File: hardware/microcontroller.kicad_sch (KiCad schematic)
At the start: 11 parts, among them U1 STM32G474QBT6

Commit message: Very minor schematic tweaks
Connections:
- net VUSB SENSE renamed VUSB_SENSE
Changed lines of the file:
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@@
+		)
+	)
+	(label "VUSB_SENSE"
+		(at 147.32 45.72 0)
+		(effects
+			(font
+				(size 1.27 1.27)
+			)
+			(justify left bottom)
 		)
 	)
@@
 		)
 	)
-	(label "VUSB SENSE"
-		(at 147.32 45.72 0)
-		(effects
-			(font
-				(size 1.27 1.27)
-			)
-			(justify left bottom)
-		)
-	)
 	(label "SWDIO"
 		(at 129.54 60.96 180)
@@
 		)
 	)
-	(label "VUSB SENSE"
+	(label "VUSB_SENSE"
 		(at 129.54 48.26 180)
 		(effects

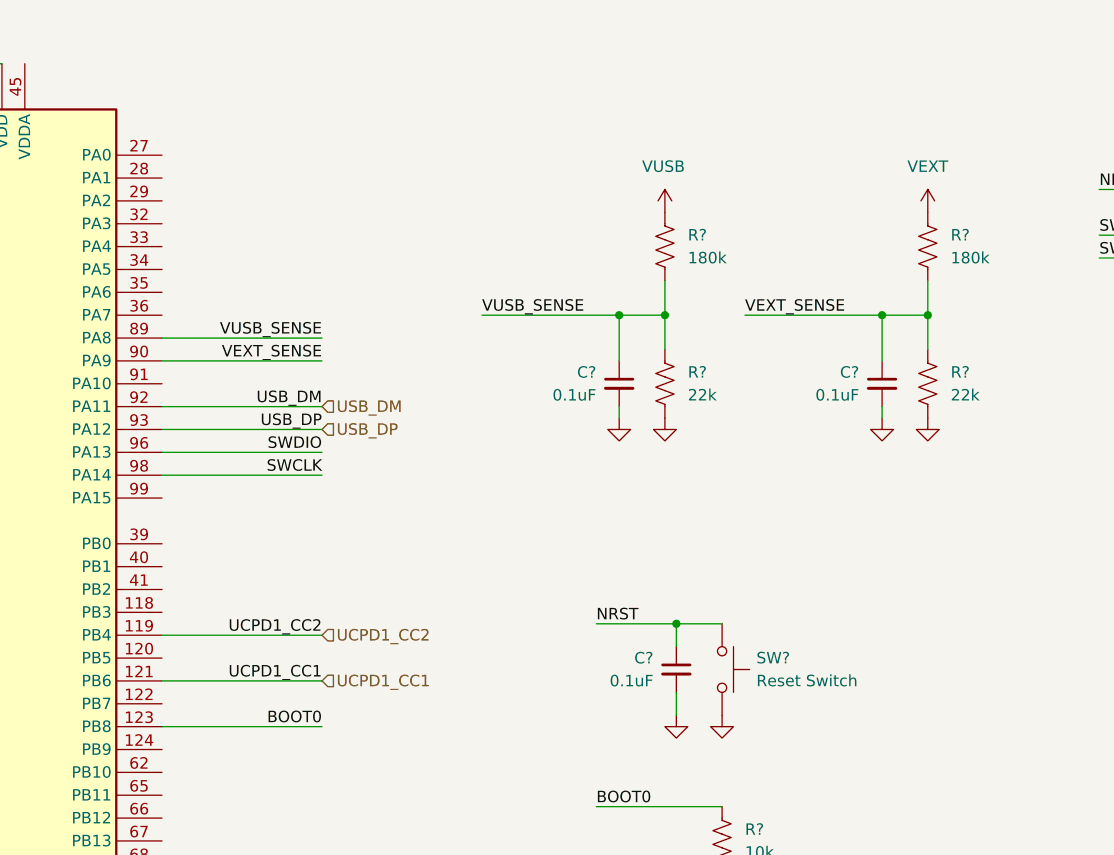
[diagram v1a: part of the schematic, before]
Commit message: Remove USB C PD and refine power input
Deleted USB C PD features due to complexity. Simplified power input schematic. Sourced PSU, connectors, crimps, and created external harness schematics.
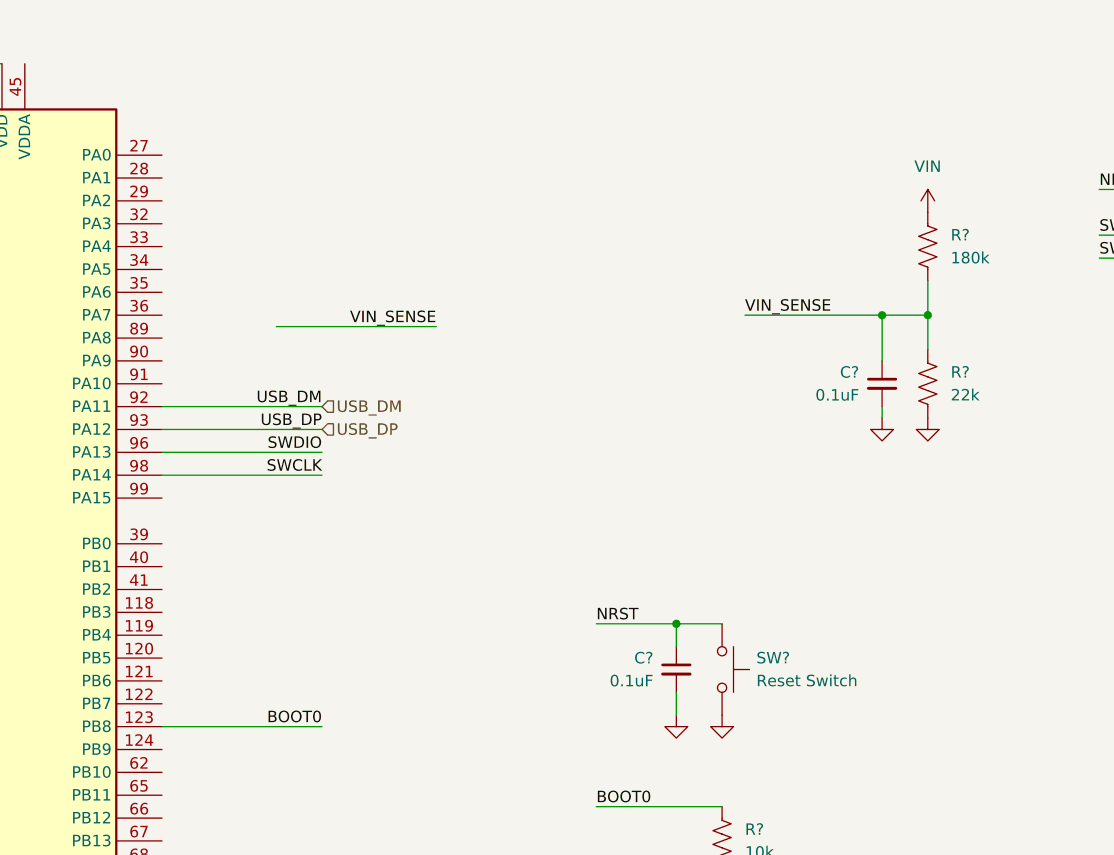
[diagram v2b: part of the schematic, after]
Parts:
- removed C?: 0.1uF, Capacitor_SMD:C_0603_1608Metric_Pad1.08x0.95mm_HandSolder, symbol Device:C_Small
- removed R?: 180k, symbol Device:R_US
- removed R?: 22k, symbol Device:R_US
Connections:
- net UCPD1_CC1: no longer names the net of U1.121 (PB6)
- net UCPD1_CC2: no longer names the net of U1.119 (PB4)
- net VEXT renamed VIN
- net VEXT_SENSE renamed VIN_SENSE
- net VIN_SENSE: no longer U1.90 (PA9)
- net VUSB_SENSE: no longer names the net of U1.89 (PA8)

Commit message: Finish power input
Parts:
- R?: footprint (none) -> Resistor_SMD:R_0603_1608Metric; Part Number (none) -> RC0603FR-0710KL; Vendor URL (none) -> https://www.digikey.com/en/products/detail/yageo/RC0603FR-0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
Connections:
- net VIN renamed VMOTOR
- net VIN_SENSE renamed VMOTOR_SENSE
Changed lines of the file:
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@@
 		)
 	)
-	(label "VIN_SENSE"
+	(label "VMOTOR_SENSE"
 		(at 176.53 45.72 0)
 		(effects
@@
 		)
 	)
+	(label "VMOTOR_SENSE"
+		(at 142.24 46.99 180)
+		(effects
+			(font
+				(size 1.27 1.27)
+			)
+			(justify right bottom)
+		)
+	)
 	(label "HSE_OSC_IN"
 		(at 38.1 66.04 0)
@@
 	(label "SWDIO"
 		(at 129.54 60.96 180)
-		(effects
-			(font
-				(size 1.27 1.27)
-			)
-			(justify right bottom)
-		)
-	)
-	(label "VIN_SENSE"
-		(at 142.24 46.99 180)
 		(effects
 			(font
@@
 	)
 	(symbol
+		(lib_id "power:VBUS")
+		(at 196.85 34.29 0)
+		(unit 1)
+		(body_style 1)
+		(exclude_from_sim no)
+		(in_bom yes)
+		(on_board yes)
+		(in_pos_files yes)
+		(dnp no)
+		(fields_autoplaced yes)
+		(property "Reference" "#PWR05"
+			(at 196.85 38.1 0)
+			(hide yes)
+			(show_name no)
+			(do_not_autoplace no)
+			(effects
+				(font
+					(size 1.27 1.27)
+				)
+			)
+		)
+		(property "Value" "VMOTOR"
+			(at 196.85 29.21 0)
+			(show_name no)
+			(do_not_autoplace no)
+			(effects
+				(font
+					(size 1.27 1.27)
+				)
+			)
+		)
+		(property "Footprint" ""
+			(at 196.85 34.29 0)
+			(hide yes)
+			(show_name no)
+			(do_not_autoplace no)
+			(effects
+				(font
+					(size 1.27 1.27)
+				)
+			)
+		)
+		(property "Datasheet" ""
+			(at 196.85 34.29 0)
+			(hide yes)
+			(show_name no)
+			(do_not_autoplace no)
+			(effects
+				(font
+					(size 1.27 1.27)
+				)
+			)
+		)
+		(property "Description" "Power symbol creates a global label with name \"VBUS\""
+			(at 196.85 34.29 0)
+			(hide yes)
+			(show_name no)
+			(do_not_autoplace no)
+			(effects
+				(font
+					(size 1.27 1.27)
+				)
+			)
+		)
+		(pin "1"
+		)
+		(instances
+			(project "stepping-stone"
+				(path "/793a882e-3f7b-468b-a863-41a1f527e1bf/d2f9d032-a5e5-45d0-b37f-4be86e3babb1"
+					(reference "#PWR05")
+					(unit 1)
+				)
+			)
+		)
+	)
+	(symbol
 		(lib_id "Device:R_US")
 		(at 196.85 38.1 0)
@@
 				(path "/793a882e-3f7b-468b-a863-41a1f527e1bf/d2f9d032-a5e5-45d0-b37f-4be86e3babb1"
 					(reference "R?")
-					(unit 1)
-				)
-			)
-		)
-	)
-	(symbol
-		(lib_id "power:VBUS")
-		(at 196.85 34.29 0)
-		(unit 1)
-		(body_style 1)
-		(exclude_from_sim no)
-		(in_bom yes)
-		(on_board yes)
-		(in_pos_files yes)
-		(dnp no)
-		(property "Reference" "#PWR035"
-			(at 196.85 38.1 0)
-			(hide yes)
-			(show_name no)
-			(do_not_autoplace no)
-			(effects
-				(font
-					(size 1.27 1.27)
-				)
-			)
-		)
-		(property "Value" "VIN"
-			(at 196.85 29.21 0)
-			(show_name no)
-			(do_not_autoplace no)
-			(effects
-				(font
-					(size 1.27 1.27)
-				)
-			)
-		)
-		(property "Footprint" ""
-			(at 196.85 34.29 0)
-			(hide yes)
-			(show_name no)
-			(do_not_autoplace no)
-			(effects
-				(font
-					(size 1.27 1.27)
-				)
-			)
-		)
-		(property "Datasheet" ""
-			(at 196.85 34.29 0)
-			(hide yes)
-			(show_name no)
-			(do_not_autoplace no)
-			(effects
-				(font
-					(size 1.27 1.27)
-				)
-			)
-		)
-		(property "Description" "Power symbol creates a global label with name \"VBUS\""
-			(at 196.85 34.29 0)
-			(hide yes)
-			(show_name no)
-			(do_not_autoplace no)
-			(effects
-				(font
-					(size 1.27 1.27)
-				)
-			)
-		)
-		(pin "1"
-		)
-		(instances
-			(project "stepping-stone"
-				(path "/793a882e-3f7b-468b-a863-41a1f527e1bf/d2f9d032-a5e5-45d0-b37f-4be86e3babb1"
-					(reference "#PWR035")
 					(unit 1)
 				)
@@
 			)
 		)
-		(property "Footprint" ""
+		(property "Footprint" "Resistor_SMD:R_0603_1608Metric"
 			(at 175.006 104.394 90)
 			(hide yes)
@@
 			)
 		)
-		(property "Datasheet" ""
+		(property "Datasheet" "https://yageogroup.com/content/datasheet/asset/file/PYU-RC_GROUP_51_ROHS_L"
 			(at 173.99 104.14 0)
 			(hide yes)
@@
 			(at 173.99 104.14 0)
 			(hide yes)
+			(show_name no)
+			(do_not_autoplace no)
+			(effects
+				(font
+					(size 1.27 1.27)
+				)
+			)
+		)
+		(property "Part Number" "RC0603FR-0710KL"
+			(at 173.99 104.14 0)
+			(hide yes)
+			(show_name no)
+			(do_not_autoplace no)
+			(effects
+				(font
+					(size 1.27 1.27)
+				)
+			)
+		)
+		(property "Vendor URL" "https://www.digikey.com/en/products/detail/yageo/RC0603FR-0710KL/726880"
+			(at 173.99 104.14 0)
+			(hide yes)

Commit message: Update LEDs
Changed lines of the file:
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@@
+		)
+	)
+	(hierarchical_label "USB_STATUS"
+		(shape output)
+		(at 135.89 50.8 0)
+		(effects
+			(font
+				(size 1.27 1.27)
+			)
+			(justify left)
 		)
 	)

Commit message: Connector Updates
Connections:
- net SWO: now reaches J?.8 (JTDO/SWO)
- net SWO: now also U1.118 (PB3)
- no-connect marks 5 -> 4
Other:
- note added: "Connector Search"

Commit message: Complete TMC2209 sheet
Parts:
- J?: footprint Connector_PinHeader_1.27mm:PinHeader_2x07_P1.27mm_Vertical_SMD -> Connector_PinHeader_1.27mm:PinHeader_2x07_P1.27mm_Vertical; Part Number (none) -> 3220-14-0100-00; Vendor URL (none) -> https://www.digikey.com/en/products/detail/cnc-tech/3220-14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
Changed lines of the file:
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@@
 			)
 		)
-		(property "Footprint" "Connector_PinHeader_1.27mm:PinHeader_2x07_P1.27mm_Vertical_SMD"
+		(property "Footprint" "Connector_PinHeader_1.27mm:PinHeader_2x07_P1.27mm_Vertical"
 			(at 236.22 44.45 0)
 			(hide yes)
@@
 			)
 		)
-		(property "Datasheet" "https://www.st.com/content/ccc/resource/technical/document/user_manual/group1/99/49/91/b6/b2/3a/46/e5/DM00526767/files/DM00526767.pdf/jcr:content/translations/en.DM00526767.pdf"
+		(property "Datasheet" "https://www.cnctech.us/pdfs/3220-XX-0100-00_.pdf"
 			(at 245.11 76.2 90)
 			(hide yes)
@@
 			)
 		)
-		(property "Description" "ST Debug Connector, standard ARM Cortex-M SWD and JTAG interface plus UART"
+		(property "Description" "Connector Header Through Hole 14 position 0.050\" (1.27mm)"
 			(at 236.22 44.45 0)
 			(hide yes)
@@
 			(at 236.22 44.45 0)
 			(hide yes)
+			(show_name no)
+			(do_not_autoplace no)
+			(effects
+				(font
+					(size 1.27 1.27)
+				)
+			)
+		)
+		(property "Part Number" "3220-14-0100-00"
+			(at 236.22 44.45 0)
+			(hide yes)
+			(show_name no)
+			(do_not_autoplace no)
+			(effects
+				(font
+					(size 1.27 1.27)
+				)
+			)
+		)
+		(property "Vendor URL" "https://www.digikey.com/en/products/detail/cnc-tech/3220-14-0100-00/3883664"
+			(at 236.22 44.45 0)
+			(hide yes)
